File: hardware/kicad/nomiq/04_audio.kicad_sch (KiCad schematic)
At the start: 9 parts, among them J5 Speaker JST-SH 2P, U5 ICS-43434, U6 MAX98357A

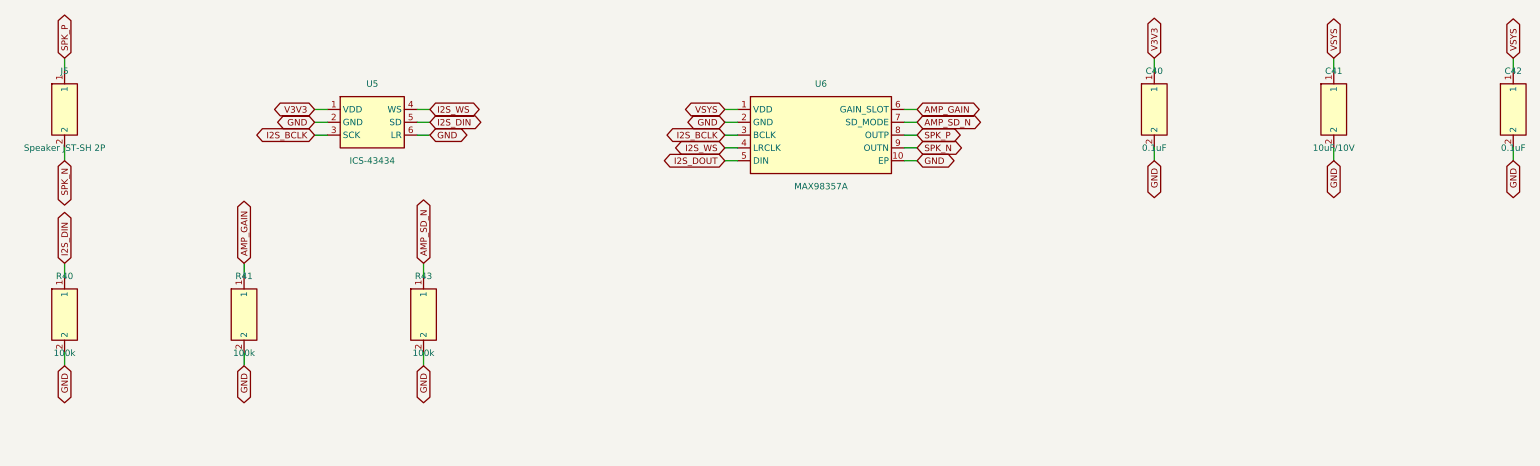
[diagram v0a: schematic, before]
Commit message: feat(sch): verified pad maps and project footprint library for all 138 parts
- fplib.py: 36 footprints from the KiCad library / Espressif library (+ TFT module),
  written to lib/nomiq.pretty and checked (make tools)
- nomiq_hw.py: per-part datasheet pin->pad maps; gen_kicad checks every pad exists
  and every copper pad is mapped (0 unverified parts)
- TPS63802 -> TPS63001 (fixed 3.3 V, KiCad DRC land pattern); BQ24074 RILIM/ITERM/TMR
  corrected to datasheet constants; TCXO 1.8 V (E) variant to match DIO3 setting
- RF blocks expanded into discrete choke, 2-section low-pass, lattice balun, DC blocks
  (PE4259 ports must be DC-free) and DNP pi tuning pads
- Display: 14-pin ILI9341 module, high-side P-FET backlight switch; microSD detect pins,
  connector mounting pads, MAX98357A NC pads

REQ-PCB-001, REQ-PCB-007

Co-Authored-By: Claude Opus 5.5 <noreply@anthropic.com>
Claude-Session: https://claude.ai/code/session_01HafD3UN2tDPG8DjCdm2PVK
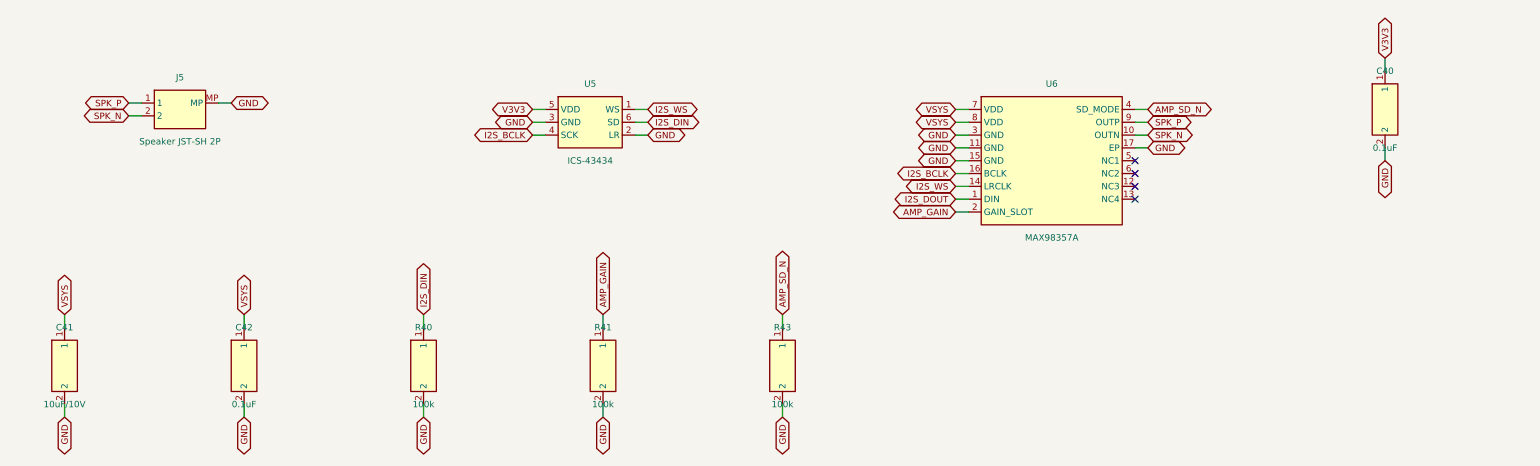
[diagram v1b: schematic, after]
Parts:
- C40, C42: footprint Capacitor_SMD:C_0402_1005Metric -> nomiq:C_0402_1005Metric
- C41: footprint Capacitor_SMD:C_0603_1608Metric -> nomiq:C_0603_1608Metric
- J5: footprint Connector_JST:JST_SH_SM02B-SRSS-TB_1x02-1MP_P1.00mm_Horizontal -> nomiq:JST_SH_SM02B-SRSS-TB_1x02-1MP_P1.00mm_Horizontal
- R40: footprint Resistor_SMD:R_0402_1005Metric -> nomiq:R_0402_1005Metric
- R41, R43: footprint Resistor_SMD:R_0402_1005Metric -> nomiq:R_0402_1005Metric; Verify yes -> (none)
- U5: footprint Sensor_Audio:InvenSense_ICS-43434-6_3.5x2.65mm -> nomiq:InvenSense_ICS-43434-6_3.5x2.65mm; PadMap unverified -> datasheet; Verify yes -> (none)
- U6: footprint Package_DFN_QFN:TQFN-16-1EP_3x3mm_P0.5mm_EP1.23x1.23mm -> nomiq:TQFN-16-1EP_3x3mm_P0.5mm_EP1.23x1.23mm; PadMap unverified -> datasheet; Verify yes -> (none)
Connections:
- net AMP_GAIN: now also U6.2 (GAIN_SLOT); no longer U6.6 (GAIN_SLOT)
- net AMP_SD_N: now also U6.4 (SD_MODE); no longer U6.7 (SD_MODE)
- net GND: now also J5.MP, U5.3 (GND), U6.11 (GND), U6.15 (GND), U6.17 (EP), U6.3 (GND); no longer U5.6 (LR), U6.10 (EP), U6.2 (GND)
- net I2S_BCLK: now also U5.4 (SCK), U6.16 (BCLK); no longer U5.3 (SCK), U6.3 (BCLK)
- net I2S_DIN: now also U5.6 (SD); no longer U5.5 (SD)
- net I2S_DOUT: now also U6.1 (DIN); no longer U6.5 (DIN)
- net I2S_WS: now also U5.1 (WS), U6.14 (LRCLK); no longer U5.4 (WS), U6.4 (LRCLK)
- net SPK_N: now also U6.10 (OUTN); no longer U6.9 (OUTN)
- net SPK_P: now also U6.9 (OUTP); no longer U6.8 (OUTP)
- net V3V3: now also U5.5 (VDD); no longer U5.1 (VDD)
- net VSYS: now also U6.7 (VDD), U6.8 (VDD); no longer U6.1 (VDD)
- no-connect marks 0 -> 4
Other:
- moved on the sheet: C40, C41, C42, R40, R41, R43, U5
